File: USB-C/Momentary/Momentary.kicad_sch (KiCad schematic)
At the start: 40 parts, among them J1 Conn_02x04_Odd_Even, J2 USB_C_Receptacle_PowerOnly_6P, J3 Conn_02x04_Odd_Even, J4 AudioJack2_Ground, J5 AudioJack2_Ground, SW1 SW_Push, U1 LM27762, U2 74HC74, U3 OPA1655, U4 TMUX4053

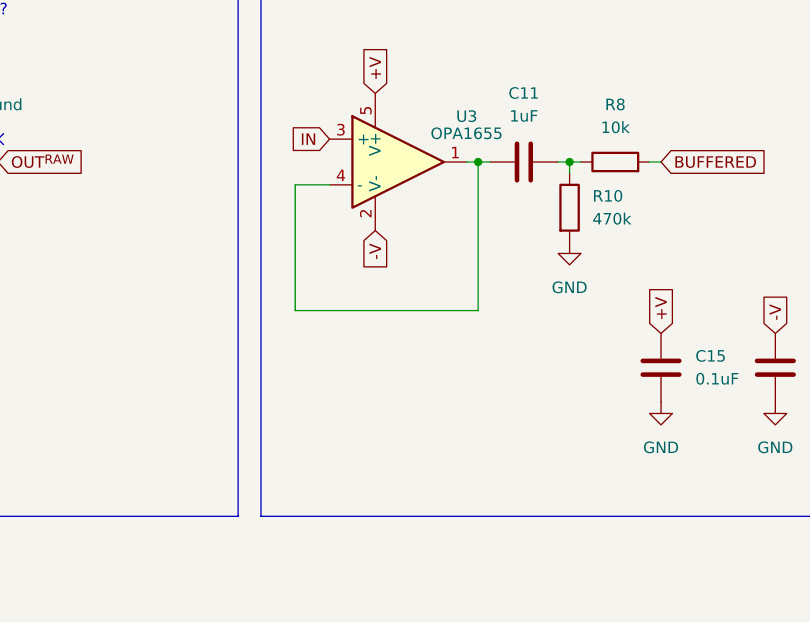
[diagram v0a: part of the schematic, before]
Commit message: Allow trimming gain on base board input buffer
Instead of just having a unity gain buffer, let's add a trim pot that
allows for higher input gain when that makes sense for the effect board.

For example, the very traditional Big Muff fuzz pedal seems to have an
input stage with roughly a voltage gain of 7x (+17dB).

Random pick: 100k trim pot with 10k resistor gives a gain range of 1-11.

Signed-off-by: Linus Torvalds <torvalds@linux-foundation.org>
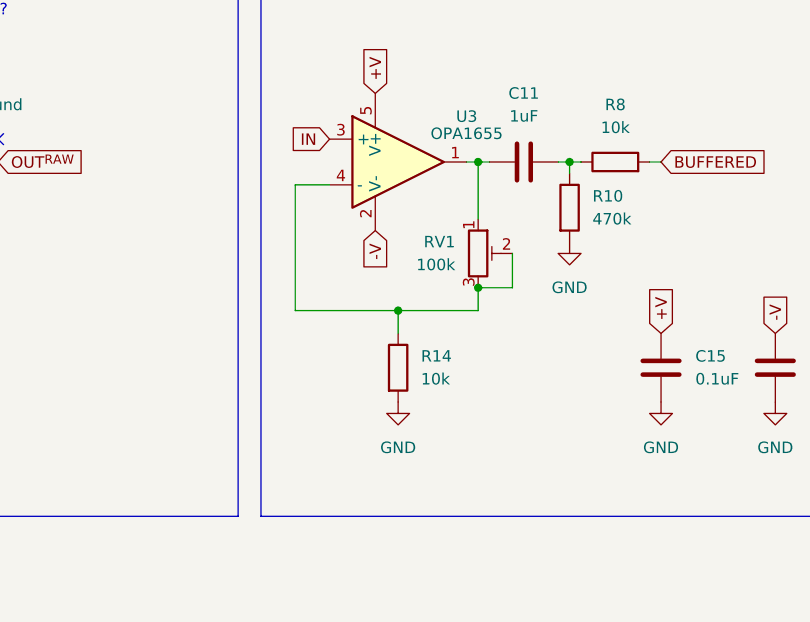
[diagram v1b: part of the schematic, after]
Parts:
- added R14: 10k, Resistor_SMD:R_0805_2012Metric_Pad1.20x1.40mm_HandSolder, symbol Device:R
- added RV1: 100k, Mylib:Bourns_3362S, symbol Device:R_Potentiometer_Trim
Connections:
- net GND: now also R14.2
- net at C11.1, U3.1: now also RV1.1; no longer U3.4 (-)
- new net: R14.1, RV1.2, RV1.3, U3.4 (-)
